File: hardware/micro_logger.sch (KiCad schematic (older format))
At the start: 26 parts, among them J4 power, J5 DM3AT-SF-PEJM5, SW2 SW_Push, U1 MIC5205-3.3, U2 TLV70218_SOT23-5, U4 ICM-20948, U5 PCA9306

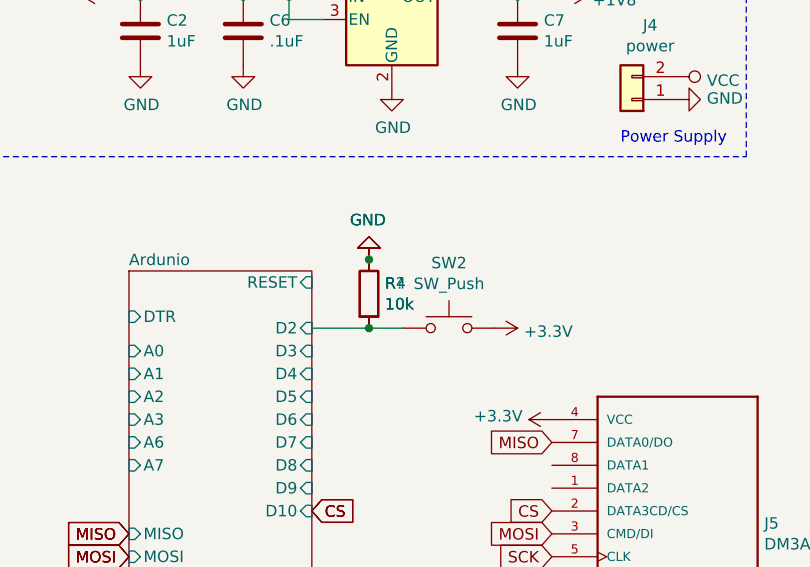
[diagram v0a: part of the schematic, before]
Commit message: added decoding app
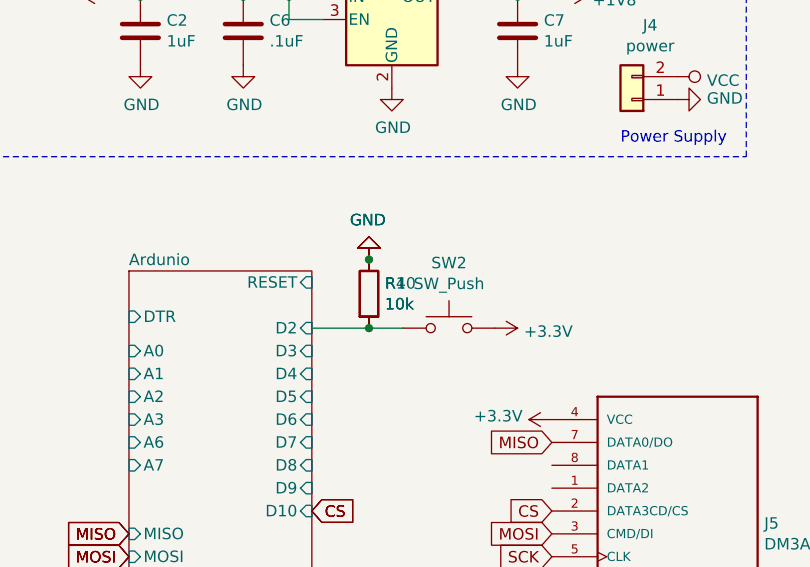
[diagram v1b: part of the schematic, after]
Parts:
- gave numbers to parts that had none: 1
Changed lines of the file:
@@
 EESchema Schematic File Version 4
 LIBS:micro_logger-cache
-EELAYER 29 0
+EELAYER 26 0
 EELAYER END
 $Descr A4 11693 8268
@@
 MISO
 $Comp
-L Device:R R?
+L Device:R R10
 U 1 1 5BF0C120
 P 2050 3100
-F 0 "R?" H 2120 3146 50  0000 L CNN
+F 0 "R10" H 2120 3146 50  0000 L CNN
 F 1 "10k" H 2120 3055 50  0000 L CNN
 F 2 "Resistor_SMD:R_0805_2012Metric" V 1980 3100 50  0001 C CNN
@@
 $EndComp
 $Comp
-L power:GND #PWR?
+L power:GND #PWR0133
 U 1 1 5BF0C12B
 P 2050 2950
-F 0 "#PWR?" H 2050 2700 50  0001 C CNN
+F 0 "#PWR0133" H 2050 2700 50  0001 C CNN
 F 1 "GND" H 2055 2777 50  0000 C CNN
 F 2 "" H 2050 2950 50  0001 C CNN
